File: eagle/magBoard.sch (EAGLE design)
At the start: 15 parts, among them J1 RJ11-6PTH, U1 ITG-3200, U2 ADXL362, U3 MAX232PTH

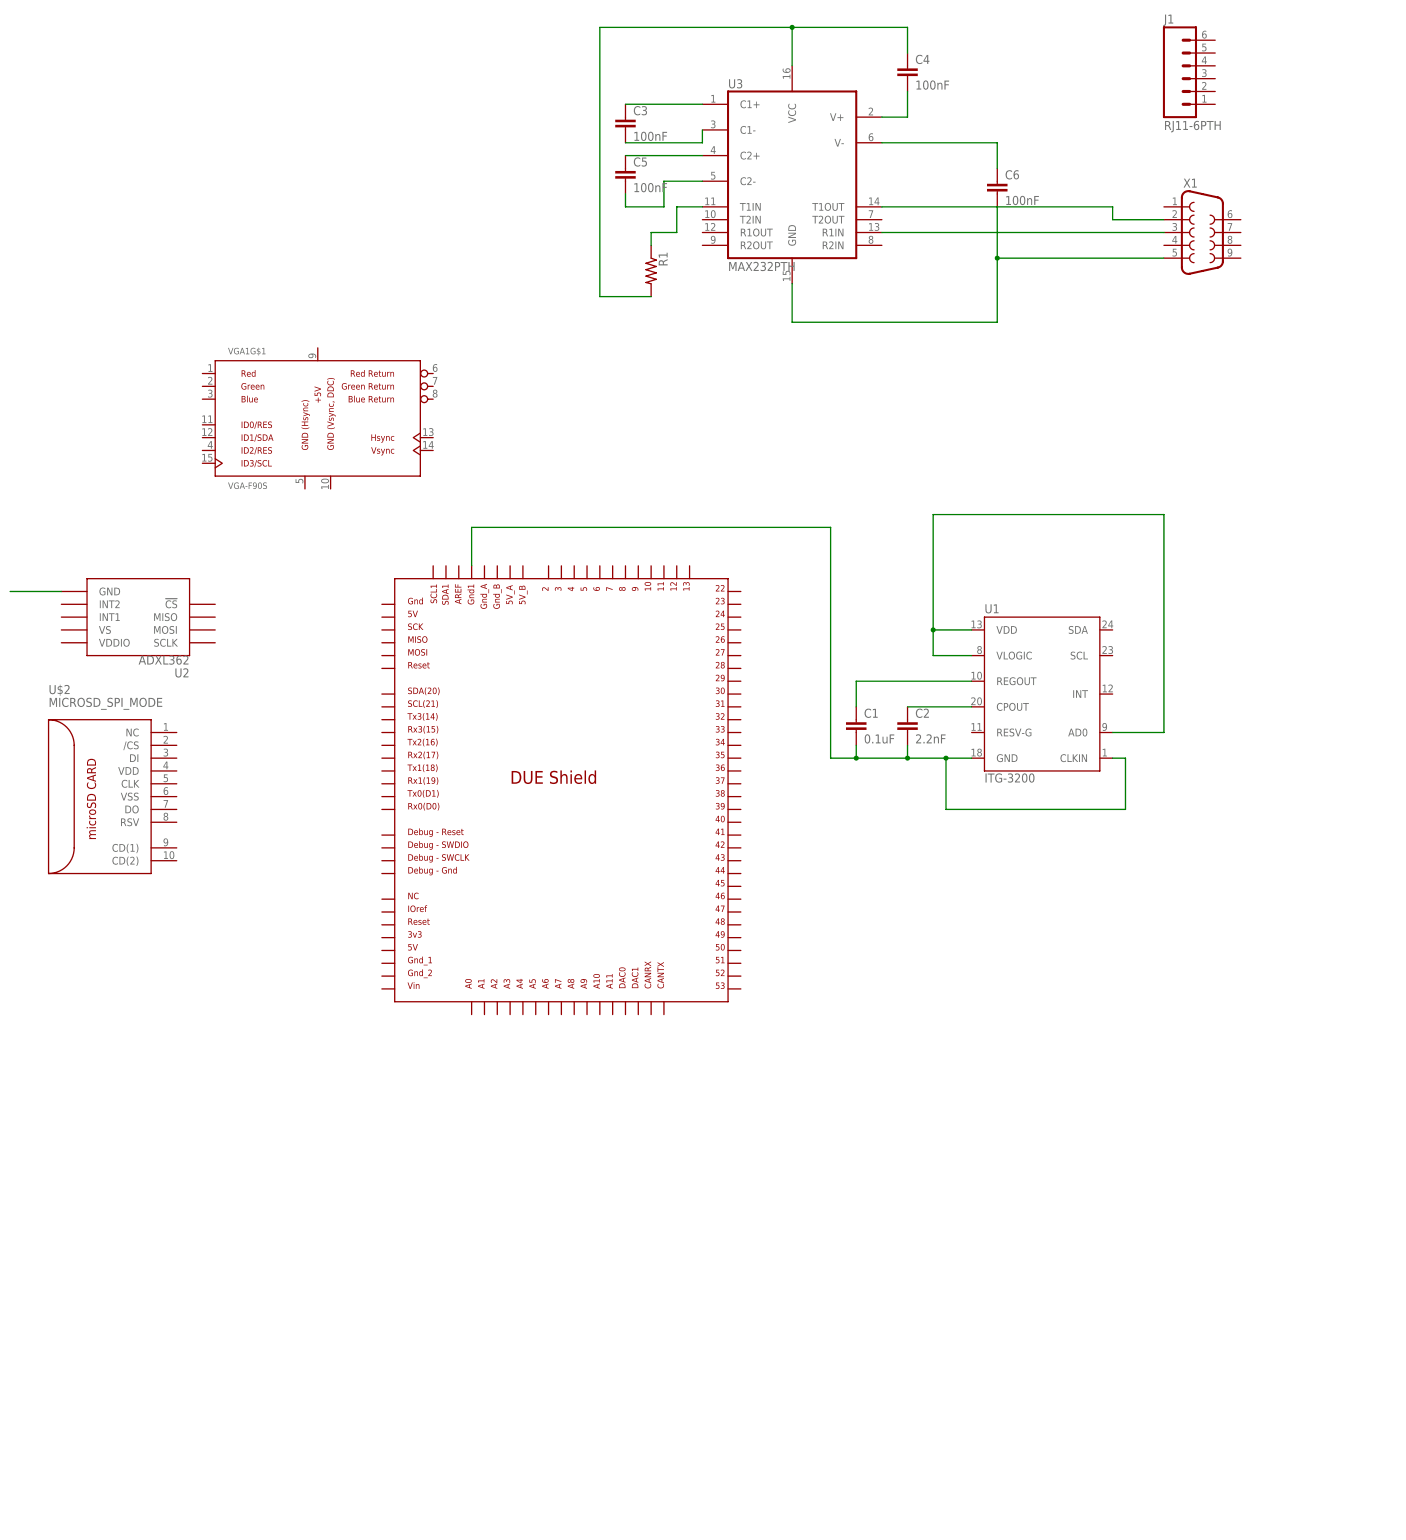
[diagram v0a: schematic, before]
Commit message: magBoard eagle file created
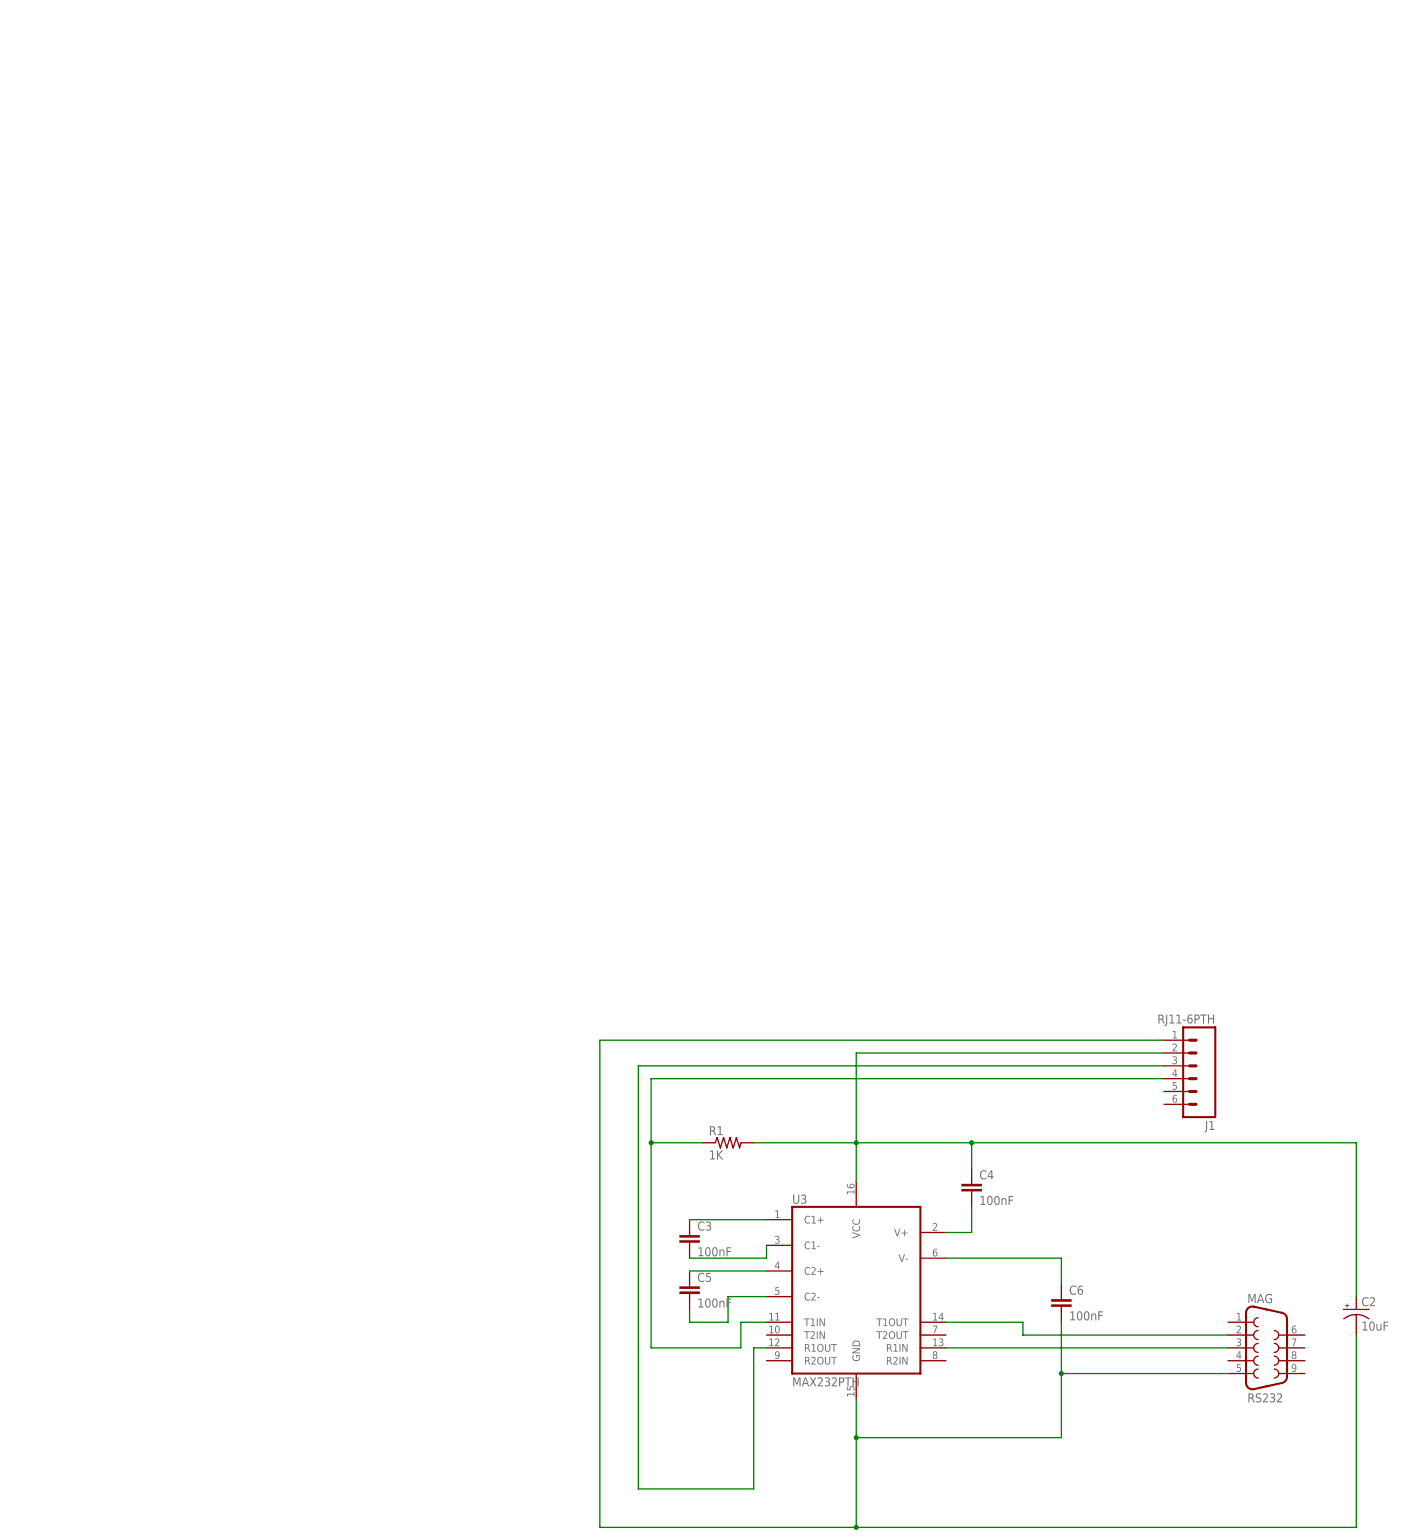
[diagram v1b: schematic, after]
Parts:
- removed C1: 0.1uF, SparkFun-Capacitors:CAPKIT
- removed U$1: DUE(NORMAL), DUElib130425:DUE(NORMAL)
- removed U$2: MICROSD_SPI_MODE, con-molex-microsd:MICROSD_SPI_MODE
- removed U1: ITG-3200, SparkFun:ITG-3200
- removed U2: ADXL362, SparkFun-Sensors:ADXL362
- removed VGA1: VGA-F90S, VideoConnectors:VGA-F90S
- removed X1: (no value), SparkFun-Connectors:DB9FEMALE
- added MAG: RS232, SparkFun-Connectors:DB9FEMALE
- C2: value 2.2nF -> 10uF; device SparkFun-Capacitors:CAPKIT -> SparkFun-Capacitors:CAP_POLPTH2
- R1: value (none) -> 1K; device resistor:R-US_0204/5 -> rcl:R-US_0204/5
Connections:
- removed net N$10: C1.2, C2.2, U$1.GND1, U1.CLKIN, U1.GND
- removed net N$11: C2.1, U1.CPOUT
- removed net N$14: R1.1, U3.T1IN
- removed net N$9: C1.1, U1.REGOUT
- net N$1: now also J1.3, U3.R1OUT; no longer U2.GND
- net N$13: now also C2.-, J1.1, MAG.5; no longer X1.5
- net N$16: now also MAG.3; no longer X1.3
- net N$17: now also MAG.2; no longer X1.2
- net N$6: now also J1.4, R1.1, U3.T1IN; no longer U1.AD0, U1.VDD, U1.VLOGIC
- net N$7: now also C2.+, J1.2
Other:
- moved on the sheet: C3, C4, C5, C6, J1, R1, U3

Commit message: updated magBoard and thesis files, added a couple boards and schematics for references or parts.
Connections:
- net N$1 renamed RX
- net N$13 renamed GND
- net N$6 renamed TX
- net N$7 renamed VH
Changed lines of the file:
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@@
 </segment>
 </net>
-<net name="N$7" class="0">
+<net name="VH" class="0">
 <segment>
 <pinref part="U3" gate="G$1" pin="VCC"/>
@@
 </segment>
 </net>
-<net name="N$13" class="0">
+<net name="GND" class="0">
 <segment>
 <pinref part="U3" gate="G$1" pin="GND"/>
@@
 </segment>
 </net>
-<net name="N$1" class="0">
+<net name="RX" class="0">
 <segment>
 <pinref part="U3" gate="G$1" pin="R1OUT"/>
@@
 </segment>
 </net>
-<net name="N$6" class="0">
+<net name="TX" class="0">
 <segment>
 <pinref part="J1" gate="G$1" pin="4"/>

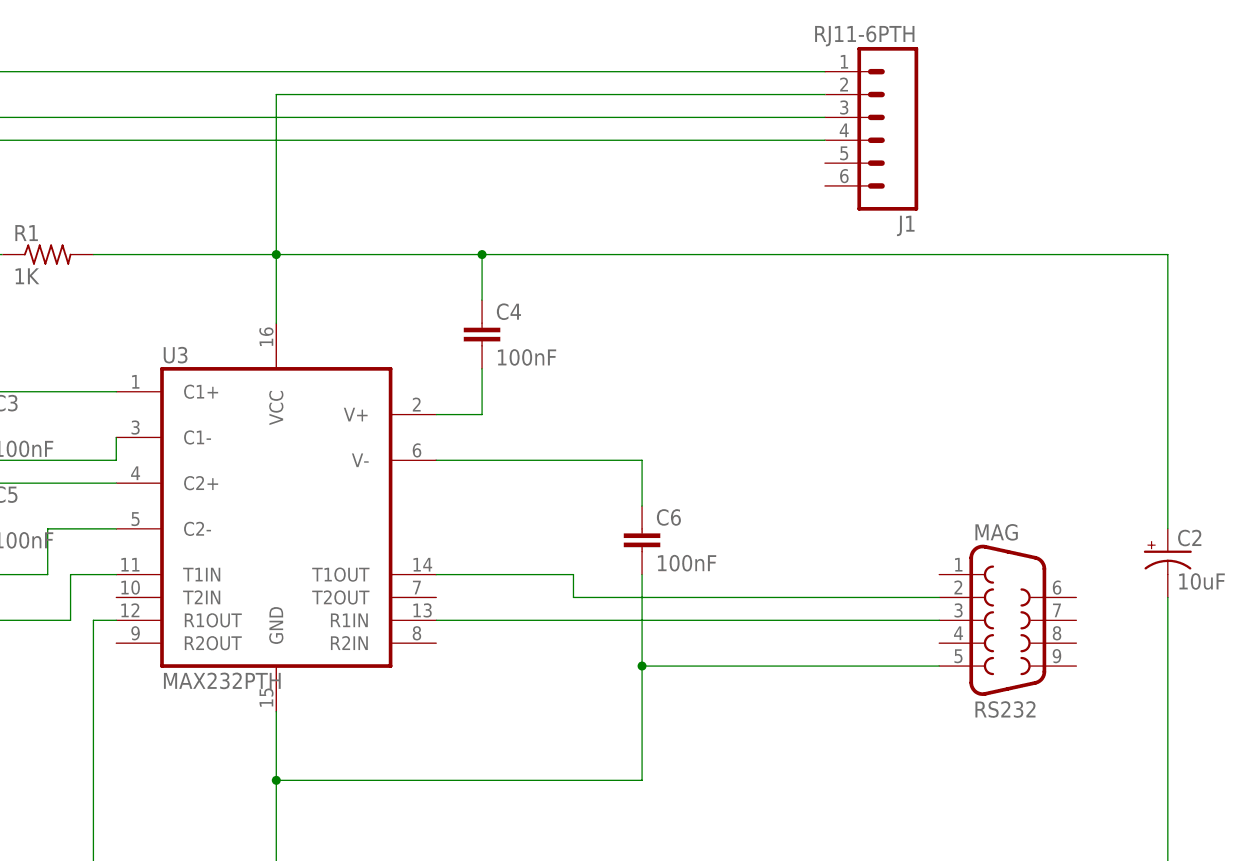
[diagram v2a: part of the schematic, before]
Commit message: made board revision to v2.0 and ready to order, pending BOM
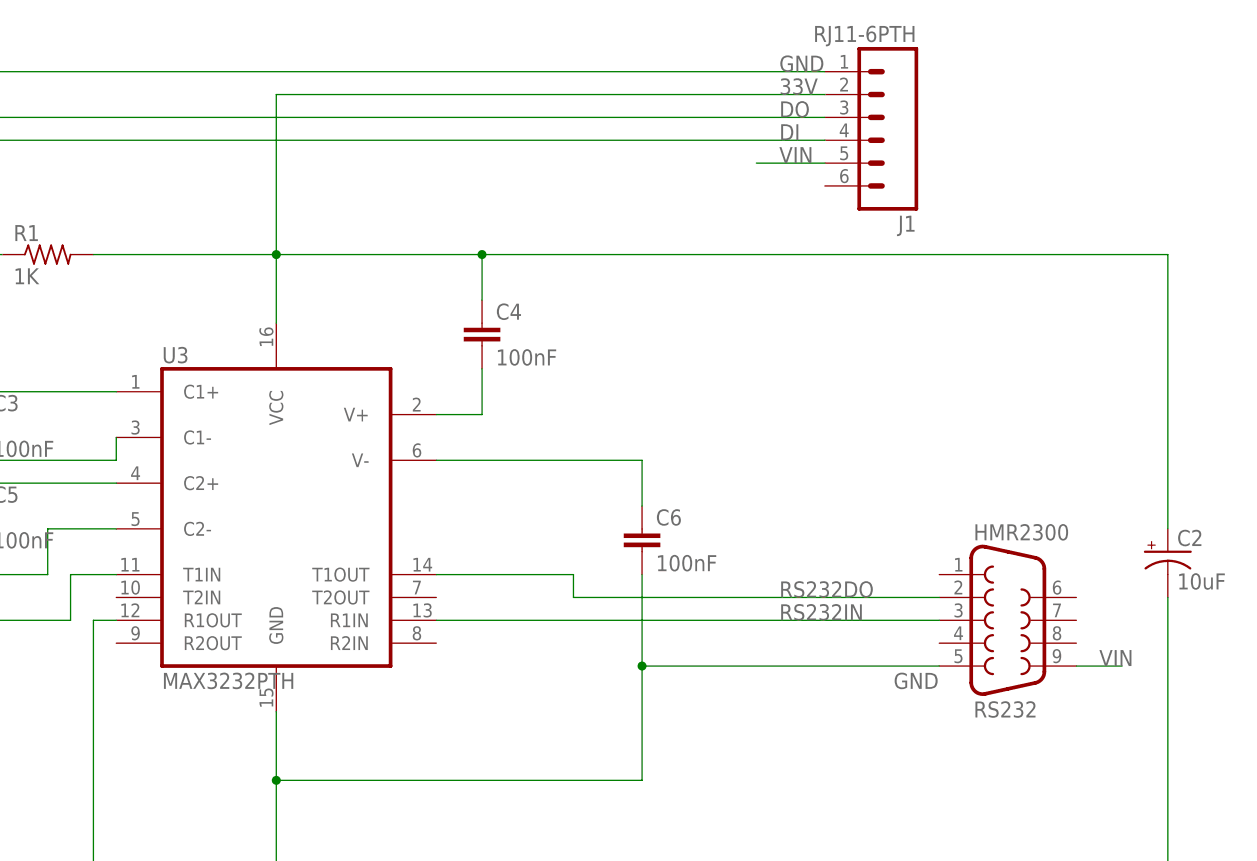
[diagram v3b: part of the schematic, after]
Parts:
- U3: value MAX232PTH -> MAX3232PTH
- renumbered MAG to HMR2300
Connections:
- net N$16 renamed RS232IN
- net N$17 renamed RS232DO
- net RX renamed DO
- net TX renamed DI
- net VH renamed 33V
- new net VIN: HMR2300.9, J1.5
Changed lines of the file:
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@@
 </classes>
 <parts>
-<part name="U3" library="SparkFun-DigitalIC" deviceset="MAX232" device="PTH"/>
+<part name="U3" library="SparkFun-DigitalIC" deviceset="MAX232" device="PTH" value="MAX3232PTH"/>
 <part name="C4" library="SparkFun-Capacitors" deviceset="CAP" device="KIT" value="100nF"/>
 <part name="C3" library="SparkFun-Capacitors" deviceset="CAP" device="KIT" value="100nF"/>
 <part name="C5" library="SparkFun-Capacitors" deviceset="CAP" device="KIT" value="100nF"/>
 <part name="C6" library="SparkFun-Capacitors" deviceset="CAP" device="KIT" value="100nF"/>
-<part name="MAG" library="SparkFun-Connectors" deviceset="DB9" device="FEMALE" value="RS232"/>
+<part name="HMR2300" library="SparkFun-Connectors" deviceset="DB9" device="FEMALE" value="RS232"/>
 <part name="J1" library="SparkFun-Connectors" deviceset="RJ11-6" device="PTH"/>
 <part name="R1" library="rcl" deviceset="R-US_" device="0204/5" value="1K"/>
@@
 <instance part="C5" gate="G$1" x="-33.02" y="-2.54"/>
 <instance part="C6" gate="G$1" x="40.64" y="-5.08"/>
-<instance part="MAG" gate="G$1" x="81.28" y="-12.7"/>
+<instance part="HMR2300" gate="G$1" x="81.28" y="-12.7"/>
 <instance part="J1" gate="G$1" x="66.04" y="43.18" rot="R180"/>
 <instance part="R1" gate="G$1" x="-25.4" y="27.94"/>
@@
 </segment>
 </net>
-<net name="VH" class="0">
+<net name="33V" class="0">
 <segment>
 <pinref part="U3" gate="G$1" pin="VCC"/>
@@
 <wire x1="99.06" y1="27.94" x2="99.06" y2="-2.54" width="0.1524" layer="91"/>
 <junction x="22.86" y="27.94"/>
+<label x="55.88" y="45.72" size="1.778" layer="95"/>
 </segment>
 </net>
@@
 <wire x1="0" y1="-30.48" x2="40.64" y2="-30.48" width="0.1524" layer="91"/>
 <wire x1="40.64" y1="-30.48" x2="40.64" y2="-17.78" width="0.1524" layer="91"/>
-<pinref part="MAG" gate="G$1" pin="5"/>
+<pinref part="HMR2300" gate="G$1" pin="5"/>
 <wire x1="73.66" y1="-17.78" x2="40.64" y2="-17.78" width="0.1524" layer="91"/>
 <wire x1="0" y1="-30.48" x2="0" y2="-48.26" width="0.1524" layer="91"/>
@@
 <wire x1="40.64" y1="-7.62" x2="40.64" y2="-17.78" width="0.1524" layer="91"/>
 <junction x="40.64" y="-17.78"/>
+<label x="55.88" y="48.26" size="1.778" layer="95"/>
+<label x="68.58" y="-20.32" size="1.778" layer="95"/>
 </segment>
 </net>
-<net name="N$16" class="0">
+<net name="RS232IN" class="0">
 <segment>
-<pinref part="MAG" gate="G$1" pin="3"/>
+<pinref part="HMR2300" gate="G$1" pin="3"/>
 <pinref part="U3" gate="G$1" pin="R1IN"/>
 <wire x1="73.66" y1="-12.7" x2="17.78" y2="-12.7" width="0.1524" layer="91"/>
+<label x="55.88" y="-12.7" size="1.778" layer="95"/>
 </segment>
 </net>
-<net name="N$17" class="0">
+<net name="RS232DO" class="0">
 <segment>
-<pinref part="MAG" gate="G$1" pin="2"/>
+<pinref part="HMR2300" gate="G$1" pin="2"/>
 <wire x1="73.66" y1="-10.16" x2="33.02" y2="-10.16" width="0.1524" layer="91"/>
 <wire x1="33.02" y1="-10.16" x2="33.02" y2="-7.62" width="0.1524" layer="91"/>
 <pinref part="U3" gate="G$1" pin="T1OUT"/>
 <wire x1="33.02" y1="-7.62" x2="17.78" y2="-7.62" width="0.1524" layer="91"/>
+<label x="55.88" y="-10.16" size="1.778" layer="95"/>
 </segment>
 </net>
-<net name="RX" class="0">
+<net name="DO" class="0">
 <segment>
 <pinref part="U3" gate="G$1" pin="R1OUT"/>
@@
 <pinref part="J1" gate="G$1" pin="3"/>
 <wire x1="60.96" y1="43.18" x2="-43.18" y2="43.18" width="0.1524" layer="91"/>
+<label x="55.88" y="43.18" size="1.778" layer="95"/>
 </segment>
 </net>
-<net name="TX" class="0">
+<net name="DI" class="0">
 <segment>
 <pinref part="J1" gate="G$1" pin="4"/>
@@
 <wire x1="-40.64" y1="27.94" x2="-30.48" y2="27.94" width="0.1524" layer="91"/>
 <junction x="-40.64" y="27.94"/>
+<label x="55.88" y="40.64" size="1.778" layer="95"/>
 </segment>
 </net>
+<net name="VIN" class="0">
+<segment>
+<pinref part="HMR2300" gate="G$1" pin="9"/>
+<wire x1="88.9" y1="-17.78" x2="93.98" y2="-17.78" width="0.1524" layer="91"/>
+<label x="91.44" y="-17.78" size="1.778" layer="95"/>
+</segment>
+<segment>
+<pinref part="J1" gate="G$1" pin="5"/>
+<wire x1="60.96" y1="38.1" x2="53.34" y2="38.1" width="0.1524" layer="91"/>
+<label x="55.88" y="38.1" size="1.778" layer="95"/>
+</segment>
+</net>
